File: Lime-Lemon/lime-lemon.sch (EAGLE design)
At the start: 66 parts

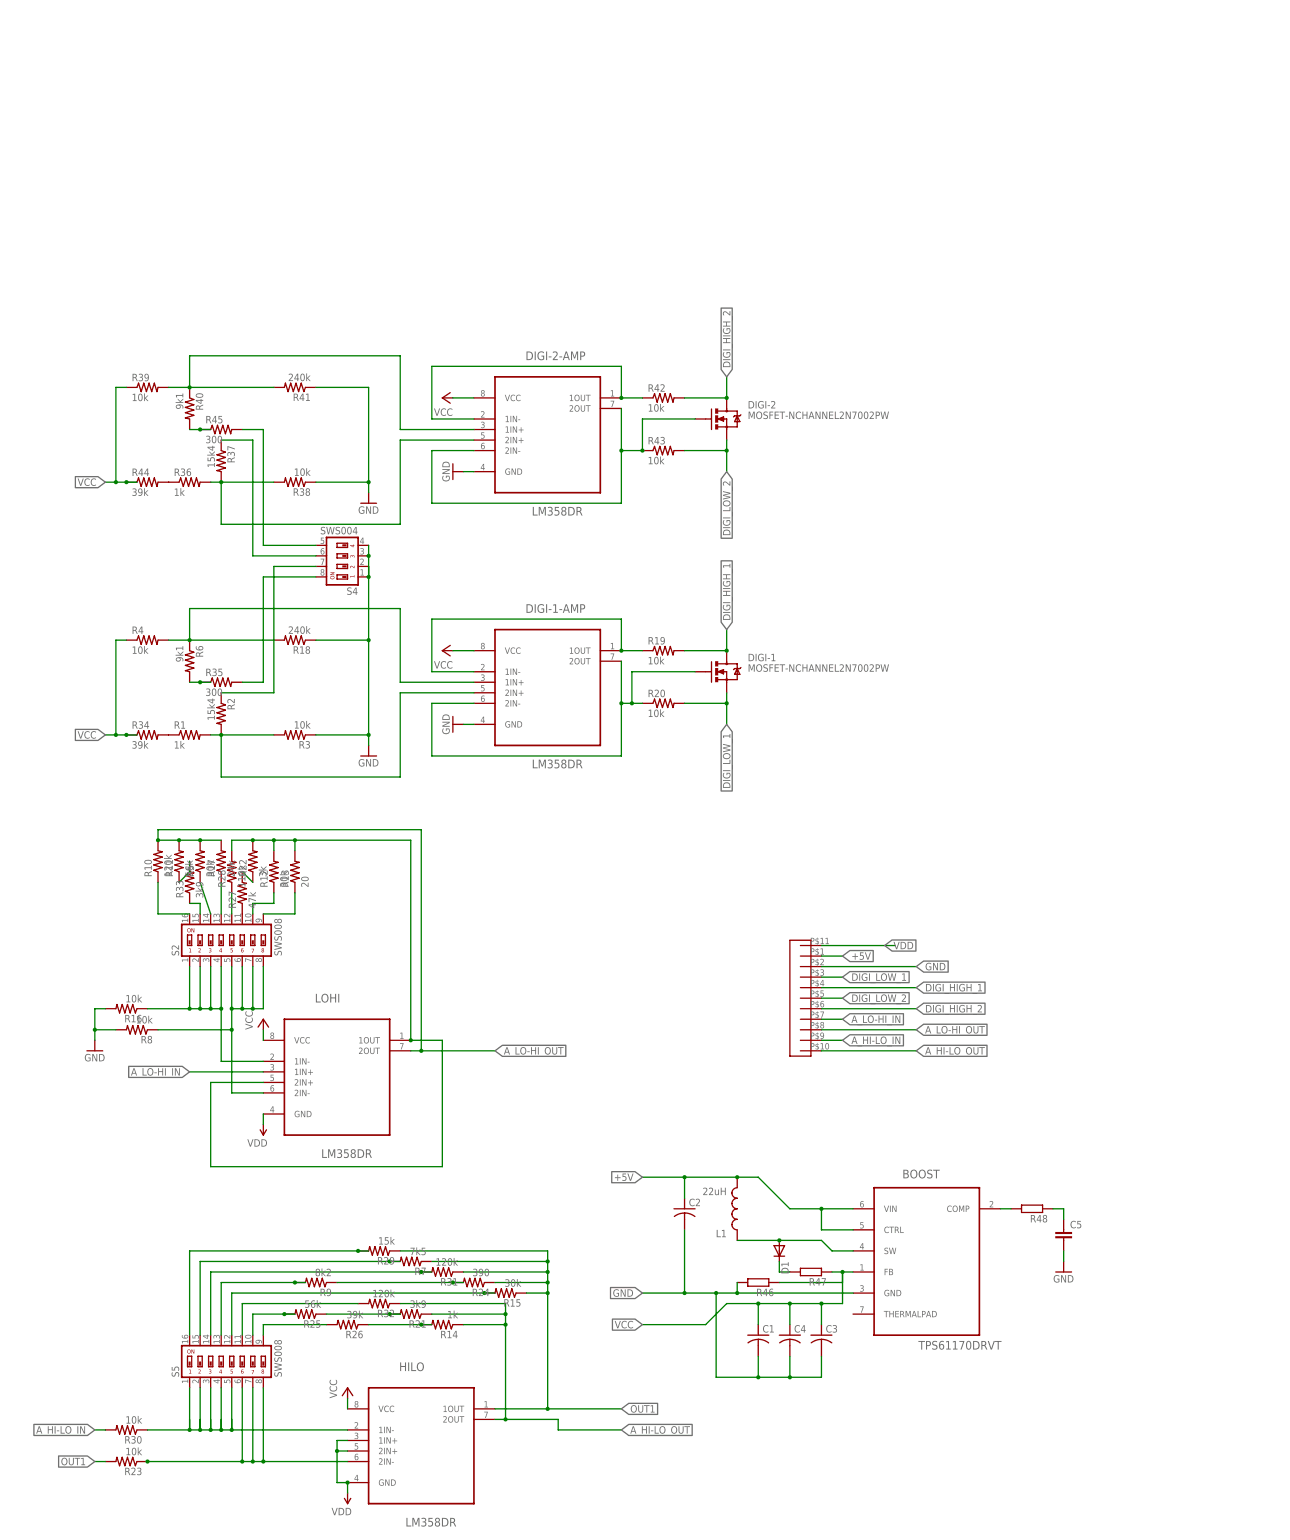
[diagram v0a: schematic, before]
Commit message: Add new lime-lemon board, schematic and inductor library
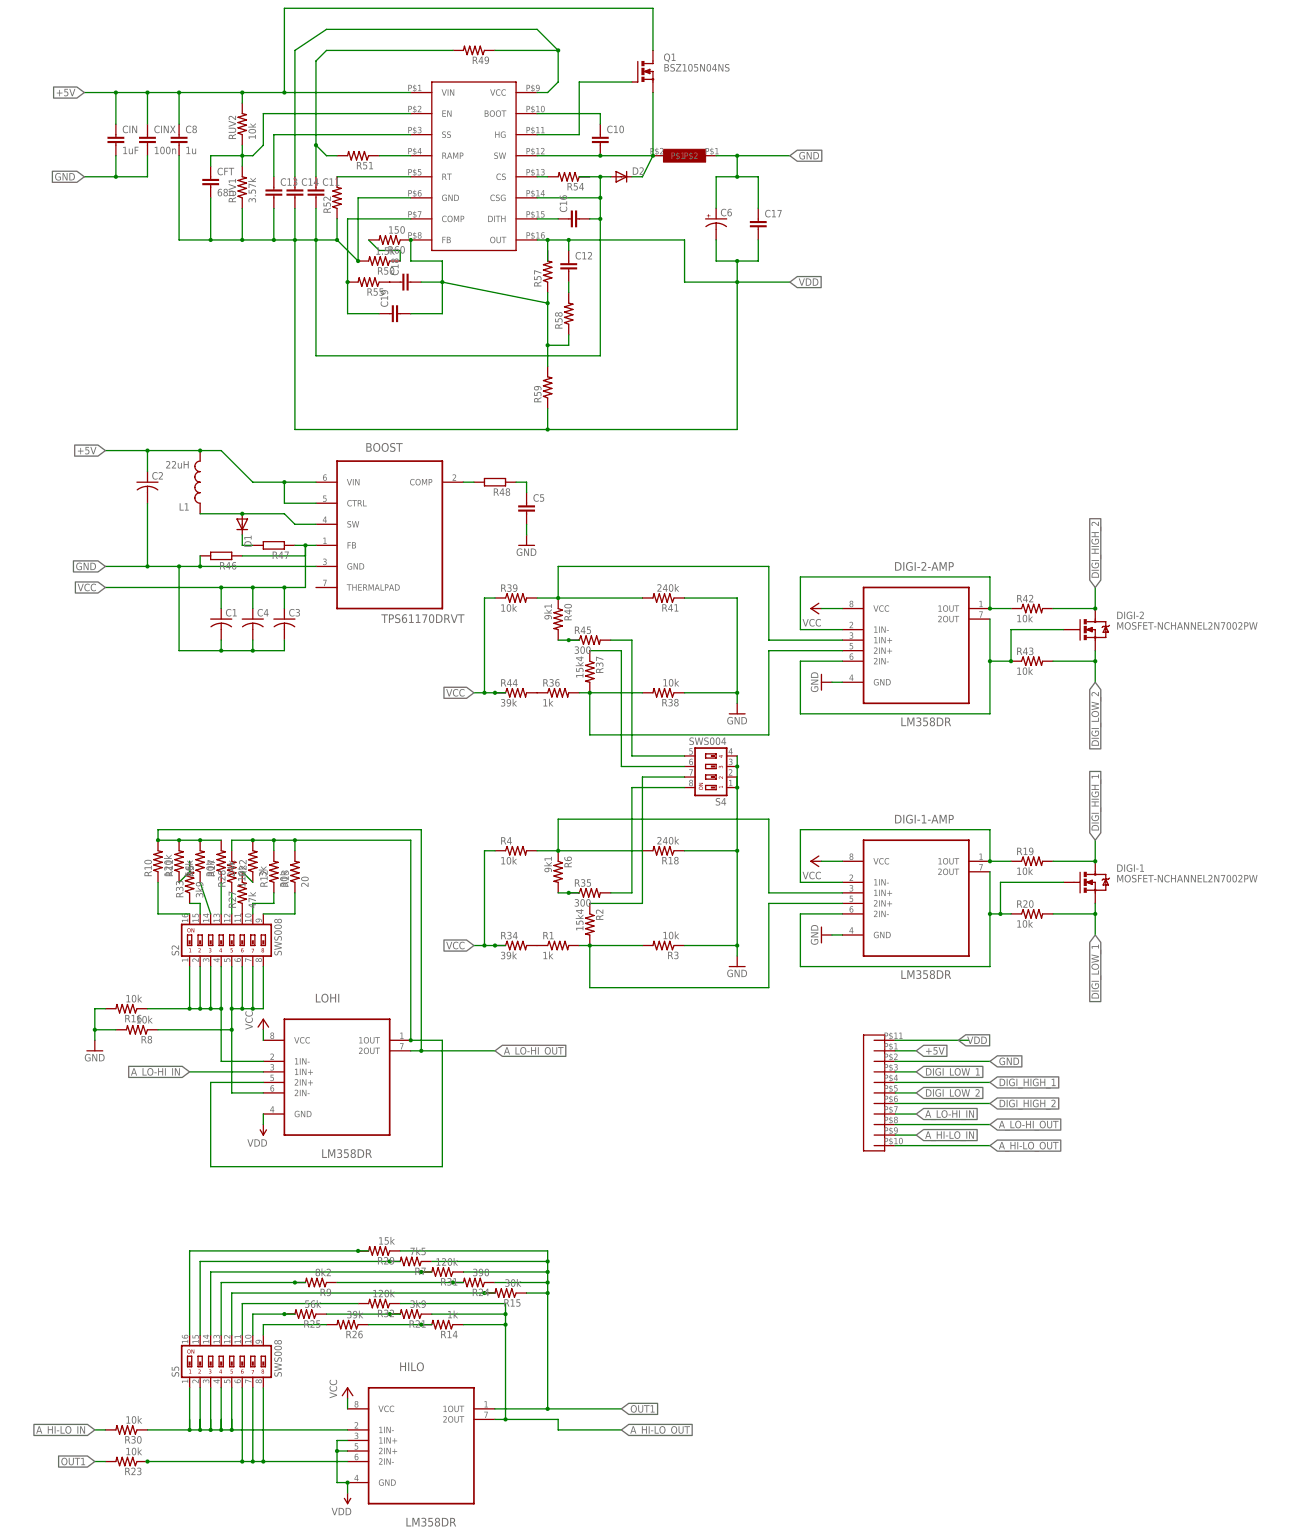
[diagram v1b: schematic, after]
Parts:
- added C10, C11, C12, C13, C14, C16, C17, C18, C19: (no value), rcl:C-EUC0805
- added C6: (no value), rcl:CPOL-USE5-5
- added C8: 1u, rcl:C-EUC0805
- added CFT: 68n, rcl:C-EUC0805
- added CIN: 1uF, rcl:C-EUC0805
- added CINX: 100n, rcl:C-EUC0805
- added D2: (no value), diode:DIODE-SOD123
- added Q1: BSZ105N04NS, transistor-power:BSZ105N04NS
- added R49, R51, R52, R54, R55, R57, R58, R59: (no value), rcl:R-US_R0805
- added R50: 1.5k, rcl:R-US_R0805
- added R60: 150, rcl:R-US_R0805
- added RUV1: 3.57k, rcl:R-US_R0805
- added RUV2: 10k, rcl:R-US_R0805
- added U$2: LM5088, Klick_custom_lm5088:LM5088
- added U$3: KLICK_INDUCTOR01, Klick_inductor01:KLICK_INDUCTOR01
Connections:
- new net N$43: CFT.1, RUV1.2, RUV2.1, U$2.EN
- new net N$45: C13.1, U$2.SS
- new net N$48: C14.1, R49.1, U$2.VCC
- new net N$52: C11.1, R49.2, R51.2
- new net N$53: R51.1, U$2.RAMP
- new net N$54: R52.2, U$2.RT
- new net N$55: C16.1, U$2.DITH
- new net N$56: C18.1, R55.1
- new net N$57: C18.2, C19.2, R57.1, R58.1, R59.2, R60.1, U$2.FB
- new net N$58: C19.1, R55.2, U$2.COMP
- new net N$59: C10.1, U$2.BOOT
- new net N$60: R54.2, U$2.CS
- new net N$61: C10.2, D2.C, Q1.S, U$2.SW, U$3.P$2
- new net N$62: R50.1, R60.2
- new net N$65: Q1.G, U$2.HG
- new net N$71: C12.2, R58.2
- net +5V: now also C8.1, CIN.1, CINX.1, Q1.D, RUV2.2, U$2.VIN
- net GND: now also C17.1, C6.+, CIN.2, CINX.2, U$3.P$1
- net VDD: now also C11.2, C12.1, C13.2, C14.2, C16.2, C17.2, C6.-, C8.2, CFT.2, D2.A, R50.2, R52.1, R59.1, RUV1.1, U$2.CSG, U$2.GND, U$2.OUT
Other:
- moved on the sheet: BOOST, C1, C2, C3, C4, C5, D1, DIGI-1, DIGI-1-AMP, DIGI-2, DIGI-2-AMP, L1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
